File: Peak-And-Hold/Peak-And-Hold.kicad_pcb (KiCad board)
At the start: 2 copper layers, 98.9 x 35.1 mm, 31 parts, among them Q1 2N6044, Q2 2N6044, Q3 2N6044, Q4 2N6044, Q5 TIP42C, U1 LM1949N_NOPB, U2 LM1949N_NOPB, U3 LM1949N_NOPB, U4 LM1949N_NOPB

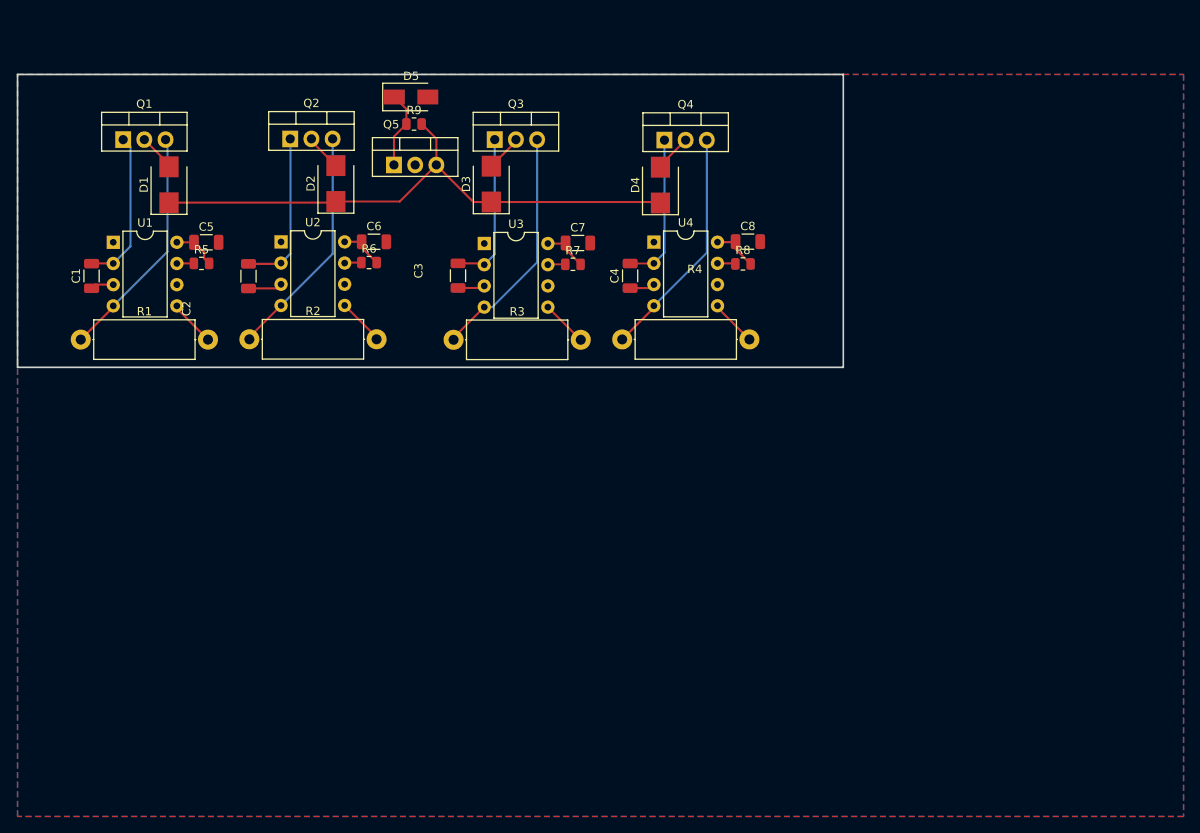
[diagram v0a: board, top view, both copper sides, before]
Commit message: added plugs
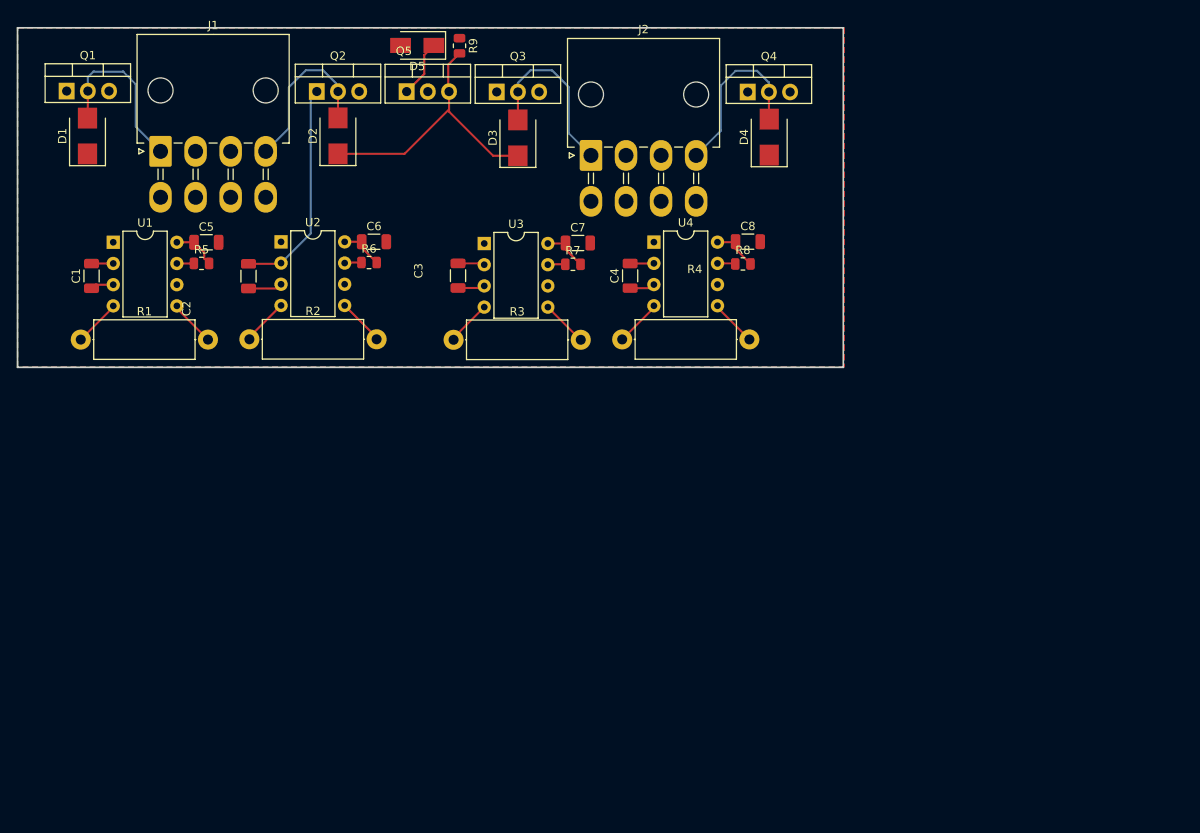
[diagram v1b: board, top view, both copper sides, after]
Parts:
- added J1: 39301080, Connector_Molex:Molex_Mini-Fit_Jr_5569-08A2_2x04_P4.20mm_Horizontal, F.Cu at (67.9, 72.7)
- added J2: 39301080, Connector_Molex:Molex_Mini-Fit_Jr_5569-08A2_2x04_P4.20mm_Horizontal, F.Cu at (119.5, 73.2)
- moved D4 14.2 mm to (140.9, 71.0)
- moved Q4 11.5 mm to (138.3, 65.6)
- moved D1 11.4 mm to (59.2, 70.9)
- moved R9 10.8 mm to (103.8, 60.1), turned to -90 degrees
- moved Q1 8.92 mm to (56.7, 65.5)
- moved Q5 8.92 mm to (97.4, 65.6)
- moved Q2 6.51 mm to (86.7, 65.5)
- moved D3 6.40 mm to (110.7, 71.1)
- moved D5 6.22 mm to (98.7, 60.0), turned to 180 degrees
- moved Q3 5.72 mm to (108.2, 65.6)
- moved D2 5.71 mm to (89.2, 70.9)
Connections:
- U1 pad 6: GND -> /LoGND
- U2 pad 6: GND -> /LoGND
- U3 pad 6: GND -> /LoGND
- U4 pad 6: GND -> /LoGND
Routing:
- net Net-(D1-Pad1): track 68.3 -> 35.7 mm
- net Net-(Q3-Pad3): track 28.7 -> 5.44 mm
- net Net-(Q1-Pad3): track 28.4 -> 5.65 mm
- net Net-(Q2-Pad3): track 28.1 -> 5.62 mm
- net Net-(Q4-Pad3): track 28.1 -> 5.61 mm
- net /INJ3OUT: track 4.40 -> 21.3 mm
- net /INJ4OUT: track 4.48 -> 21.1 mm
- net /INJ1OUT: track 4.48 -> 20.8 mm
- net Net-(C1-Pad2): track 18.7 -> 2.61 mm
- net /INJ2OUT: track 4.42 -> 20.2 mm
- net Net-(C3-Pad2): track 18.7 -> 3.21 mm
- net Net-(C4-Pad2): track 18.1 -> 2.85 mm
- net Net-(C2-Pad2): track 19.3 -> 26.3 mm
- net Net-(D5-Pad1): track 9.36 -> 6.89 mm
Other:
- board size 98.9 x 35.1 mm -> 98.9 x 40.7 mm

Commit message: Update Peak-And-Hold.kicad_pcb
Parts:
- moved R8 2.50 mm to (140.2, 86.2)
- moved C8 1.93 mm to (140.2, 83.8)
- moved U4 1.60 mm to (128.6, 83.5)
- moved R4 1.33 mm to (124.6, 95.5)
- moved C4 0.59 mm to (124.8, 87.7)
- moved C7 0.15 mm to (117.9, 83.8)
- moved R7 0.12 mm to (117.3, 86.4)
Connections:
- J1 pad 6: unconnected-(J1-Pad6) -> /LoGND
- J2 pad 7: unconnected-(J2-Pad7) -> /LoGND
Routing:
- net /LoGND: track 0.00 -> 70.5 mm
- net /5v: track 8.36 -> 77.8 mm
- net Net-(D1-Pad1): track 35.7 -> 101.9 mm
- net Net-(Q4-Pad3): track 5.61 -> 38.4 mm
- net Net-(Q2-Pad3): track 5.62 -> 35.1 mm
- net Net-(Q3-Pad3): track 5.44 -> 34.7 mm
- net Net-(Q1-Pad3): track 5.65 -> 33.4 mm
- net Net-(C4-Pad2): track 2.85 -> 28.4 mm
- net /INJ3: track 0.00 -> 23.9 mm
- net Net-(C3-Pad2): track 3.21 -> 26.3 mm
- net Net-(C1-Pad2): track 2.61 -> 25.6 mm
- net /INJ1: track 0.00 -> 17.3 mm
- net /INJ2: track 0.00 -> 13.3 mm
- net /INJ4: track 0.00 -> 13.0 mm
- net /INJ2OUT: track 20.2 -> 28.0 mm
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
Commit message: finished off
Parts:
- moved D5 2.33 mm to (96.4, 60.2)
- moved R9 1.51 mm to (102.2, 60.0), turned to 0 degrees
- moved D1 0.63 mm to (59.3, 71.5)
- moved Q1 0.42 mm to (56.6, 65.9)
- moved U4 0.37 mm to (129.0, 83.6)
- moved R3 0.23 mm to (103.0, 95.5)
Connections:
- J1 pad 5: /5v -> GND
- J1 pad 8: GND -> /5v
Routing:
- net /5v: track 77.8 -> 67.0 mm
- net Net-(Q4-Pad3): track 38.4 -> 48.2 mm
- net Net-(Q1-Pad3): track 33.4 -> 42.7 mm
- net Net-(Q2-Pad3): track 35.1 -> 42.8 mm
- net Net-(Q3-Pad3): track 34.7 -> 41.6 mm
- net Net-(D5-Pad1): track 6.89 -> 8.86 mm
- net /INJ2: track 13.3 -> 15.3 mm
- net /LoGND: track 70.5 -> 72.2 mm
- net Net-(D1-Pad1): track 101.9 -> 102.7 mm
- net /INJ1OUT: track 28.0 -> 28.6 mm
- net GND: vias 101 -> 151
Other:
- board text added: "InjOut1 - Inj1 - Inj2 - InjOut2 HighGND - LowGND - LowGND - 5V"
- board text added: "InjOut3 - Inj3 - Inj4 - InjOut4 HighGND - LowGND - LowGND - 5V"
- board text added: "Peak and Hold Driver FutureProofPerformance.com 2022"

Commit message: Fabrication Ready
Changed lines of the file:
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@@
       (drillshape 0)
       (scaleselection 1)
-      (outputdirectory "Fabrication/Gerbers/")
+      (outputdirectory "Fabrication/")
     )
   )
@@
   (segment (start 124.783006 86.210688) (end 124.844279 86.149415) (width 0.762) (layer "F.Cu") (net 8))
   (segment (start 124.844279 86.149415) (end 128.9709 86.149415) (width 0.762) (layer "F.Cu") (net 8))
-  (segment (start 129.112515 86.111767) (end 129.008548 86.111767) (width 0.762) (layer "B.Cu") (net 8))
-  (segment (start 137.85883 73.652119) (end 137.85883 76.852539) (width 0.762) (layer "B.Cu") (net 8))
-  (segment (start 138.279781 73.231168) (end 137.85883 73.652119) (width 0.762) (layer "B.Cu") (net 8))
-  (segment (start 130.58315 84.641132) (end 129.112515 86.111767) (width 0.762) (layer "B.Cu") (net 8))
-  (segment (start 138.279781 65.60143) (end 138.279781 73.231168) (width 0.762) (layer "B.Cu") (net 8))
-  (segment (start 130.58315 84.128219) (end 130.58315 84.641132) (width 0.762) (layer "B.Cu") (net 8))
-  (segment (start 137.85883 76.852539) (end 130.58315 84.128219) (width 0.762) (layer "B.Cu") (net 8))
+  (segment (start 137.586723 76.730266) (end 131.08205 83.234939) (width 0.762) (layer "B.Cu") (net 8))
+  (segment (start 131.08205 83.234939) (end 131.08205 84.038265) (width 0.762) (layer "B.Cu") (net 8))
+  (segment (start 138.279781 65.60143) (end 137.586723 66.294488) (width 0.762) (layer "B.Cu") (net 8))
+  (segment (start 131.08205 84.038265) (end 129.008548 86.111767) (width 0.762) (layer "B.Cu") (net 8))
+  (segment (start 137.586723 66.294488) (end 137.586723 76.730266) (width 0.762) (layer "B.Cu") (net 8))
   (segment (start 71.944909 83.60936) (end 73.169429 84.83388) (width 0.762) (layer "F.Cu") (net 9))
   (segment (start 73.169429 84.83388) (end 73.169429 85.555241) (width 0.762) (layer "F.Cu") (net 9))
@@
   (segment (start 127.299217 91.191767) (end 129.008548 91.191767) (width 0.762) (layer "F.Cu") (net 23))
   (segment (start 124.557963 95.466909) (end 124.557963 93.933021) (width 0.762) (layer "F.Cu") (net 23))
+  (segment (start 143.359781 73.467893) (end 143.326545 73.501129) (width 2) (layer "B.Cu") (net 23))
+  (segment (start 133.134911 83.943831) (end 133.134911 92.675437) (width 2) (layer "B.Cu") (net 23))
+  (segment (start 133.134911 92.675437) (end 130.343439 95.466909) (width 2) (layer "B.Cu") (net 23))
   (segment (start 130.343439 95.466909) (end 124.557963 95.466909) (width 2) (layer "B.Cu") (net 23))
-  (segment (start 140.881063 76.297752) (end 132.662569 84.516246) (width 2) (layer "B.Cu") (net 23))
-  (segment (start 132.662569 93.147779) (end 130.343439 95.466909) (width 2) (layer "B.Cu") (net 23))
-  (segment (start 143.359781 73.802651) (end 140.881063 76.281369) (width 2) (layer "B.Cu") (net 23))
-  (segment (start 143.359781 65.60143) (end 143.359781 73.802651) (width 2) (layer "B.Cu") (net 23))
-  (segment (start 140.881063 76.281369) (end 140.881063 76.297752) (width 2) (layer "B.Cu") (net 23))
-  (segment (start 132.662569 84.516246) (end 132.662569 93.147779) (width 2) (layer "B.Cu") (net 23))
+  (segment (start 143.326545 73.501129) (end 143.326545 73.752197) (width 2) (layer "B.Cu") (net 23))
+  (segment (start 143.326545 73.752197) (end 133.134911 83.943831) (width 2) (layer "B.Cu") (net 23))
+  (segment (start 143.359781 65.60143) (end 143.359781 73.467893) (width 2) (layer "B.Cu") (net 23))
   (segment (start 116.4355 86.36) (end 116.37096 86.29546) (width 0.762) (layer "F.Cu") (net 24))
   (segment (start 132.102787 81.472502) (end 132.083362 81.491927) (width 0.762) (layer "F.Cu") (net 24))
